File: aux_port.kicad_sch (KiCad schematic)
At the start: 29 parts, among them IC1 ECP5-BGA256, J5 MEZZANINE, U11 USB3343-CP, U12 FUSB302B, U14 DPO2036

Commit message: rename libraries from luna to cynthion
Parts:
- D15: footprint luna:DFN1006-2 -> cynthion:DFN1006-2
- IC1: footprint luna:lattice_cabga256 -> cynthion:lattice_cabga256
- J5: footprint luna:Amphenol_10132798-03 -> cynthion:Amphenol_10132798-03
- U14: footprint luna:Diodes_UQFN2020-12_Type-B -> cynthion:Diodes_UQFN2020-12_Type-B
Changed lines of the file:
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@@
     (property "Reference" "J5" (id 0) (at 92.71 57.2602 0))
     (property "Value" "MEZZANINE" (id 1) (at 92.71 59.7971 0))
-    (property "Footprint" "luna:Amphenol_10132798-03" (id 2) (at 93.98 80.01 0)
+    (property "Footprint" "cynthion:Amphenol_10132798-03" (id 2) (at 93.98 80.01 0)
       (effects (font (size 1.27 1.27)) hide)
     )
@@
     (property "Reference" "U14" (id 0) (at 233.045 61.121 0))
     (property "Value" "DPO2036" (id 1) (at 233.045 63.6579 0))
-    (property "Footprint" "luna:Diodes_UQFN2020-12_Type-B" (id 2) (at 233.045 73.66 0)
+    (property "Footprint" "cynthion:Diodes_UQFN2020-12_Type-B" (id 2) (at 233.045 73.66 0)
       (effects (font (size 1.27 1.27)) hide)
     )
@@
       (effects (font (size 1.27 1.27)) (justify right))
     )
-    (property "Footprint" "luna:lattice_cabga256" (id 2) (at -53.34 7.62 0)
+    (property "Footprint" "cynthion:lattice_cabga256" (id 2) (at -53.34 7.62 0)
       (effects (font (size 1.27 1.27)) (justify left) hide)
     )
@@
       (effects (font (size 1.27 1.27)) (justify left))
     )
-    (property "Footprint" "luna:DFN1006-2" (id 2) (at 240.665 35.56 0)
-      (effects (font (size 1.27 1.27)) hide)
-    )
+    (property "Footprint" "cynthion:DFN1006-2" (id 2) (at 240.665 35.56 0)
+      (effects (font (size 1.27 1.27)) hide)
+    )

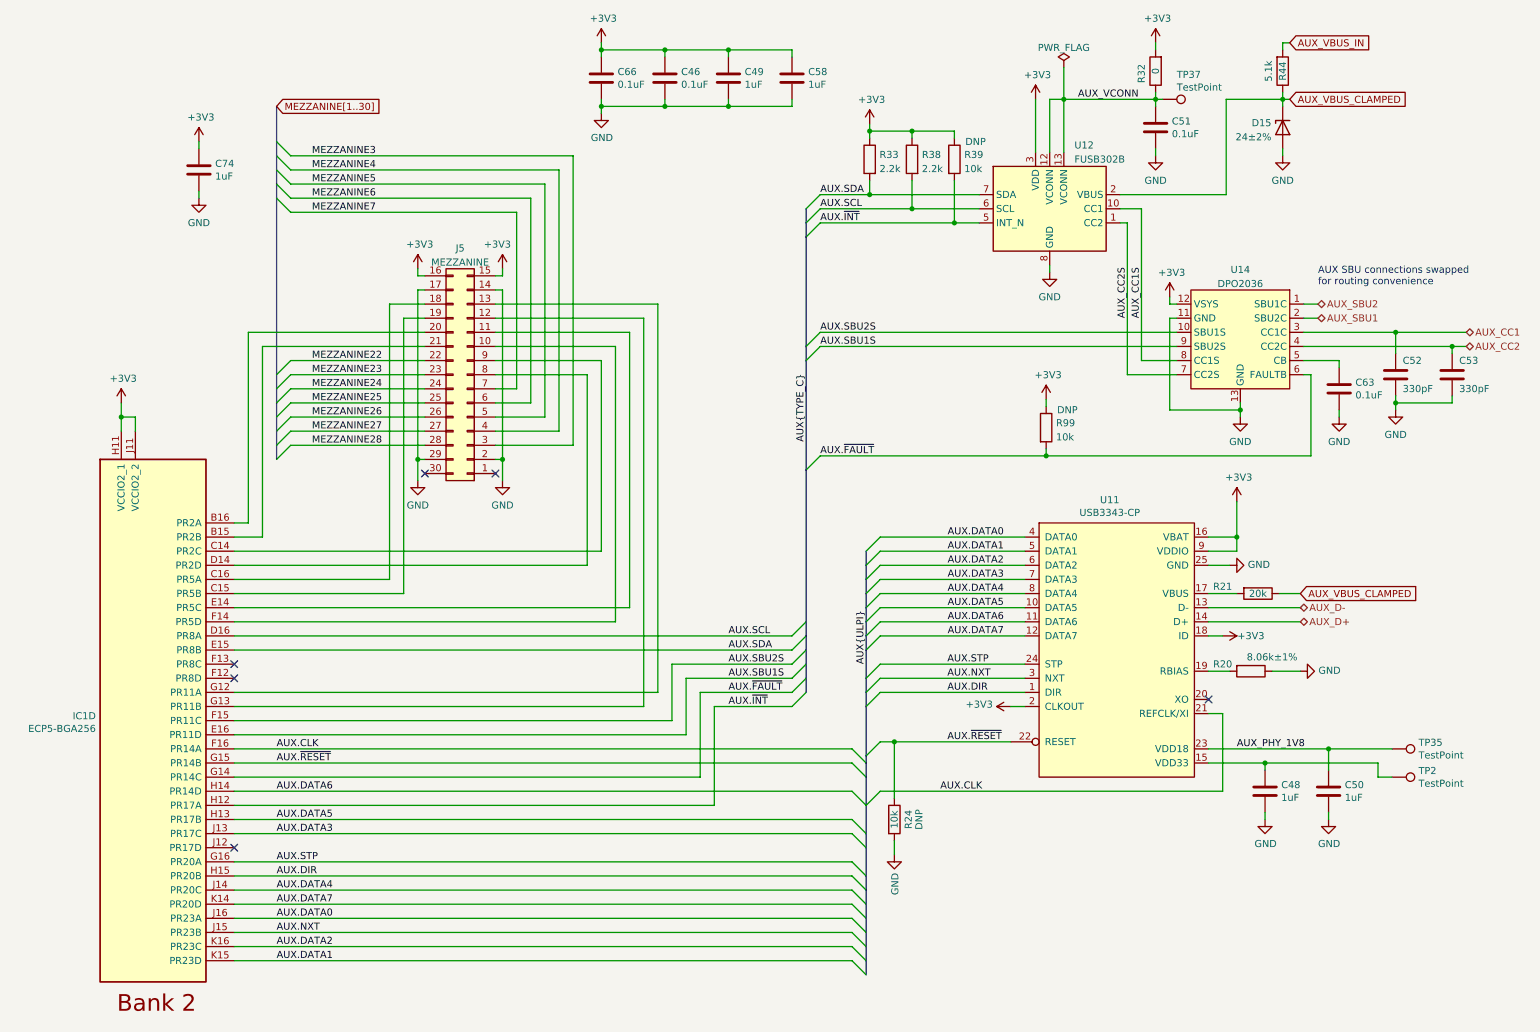
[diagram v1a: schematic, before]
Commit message: Move AUX ULPI signals to F.Cu
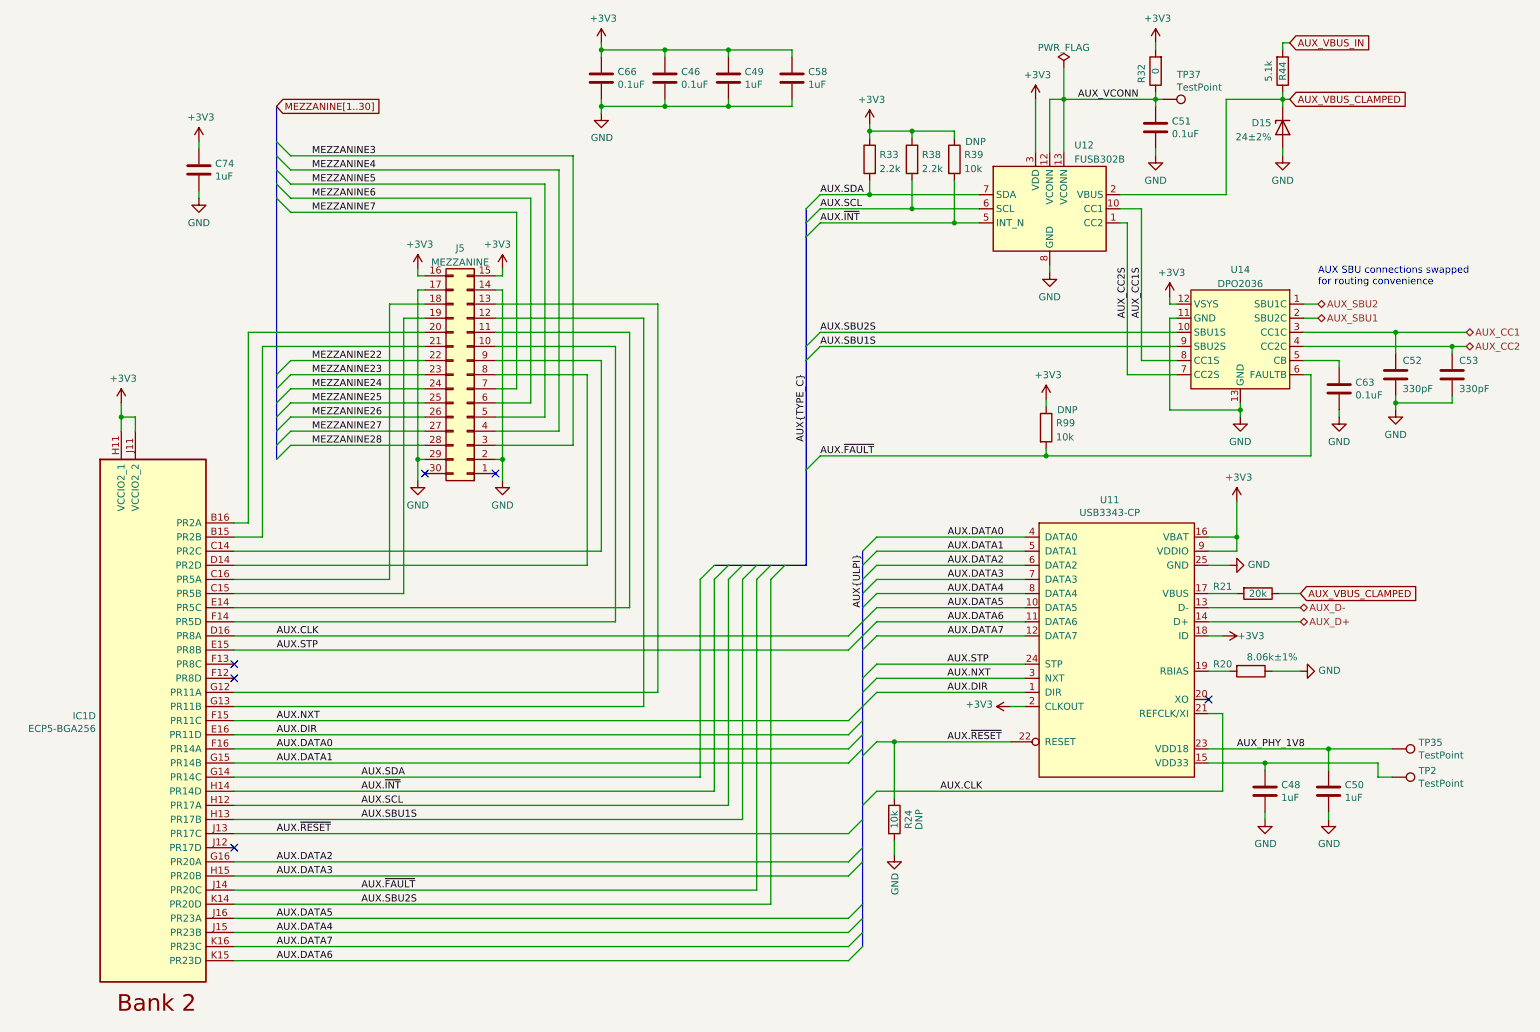
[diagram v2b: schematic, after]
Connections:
- net AUX.CLK: now also IC1.D16 (PR8A); no longer IC1.F16 (PR14A)
- net AUX.DATA0: now also IC1.F16 (PR14A); no longer IC1.J16 (PR23A)
- net AUX.DATA1: now also IC1.G15 (PR14B); no longer IC1.K15 (PR23D)
- net AUX.DATA2: now also IC1.G16 (PR20A); no longer IC1.K16 (PR23C)
- net AUX.DATA3: now also IC1.H15 (PR20B); no longer IC1.J13 (PR17C)
- net AUX.DATA4: now also IC1.J15 (PR23B); no longer IC1.J14 (PR20C)
- net AUX.DATA5: now also IC1.J16 (PR23A); no longer IC1.H13 (PR17B)
- net AUX.DATA6: now also IC1.K15 (PR23D); no longer IC1.H14 (PR14D)
- net AUX.DATA7: now also IC1.K16 (PR23C); no longer IC1.K14 (PR20D)
- net AUX.DIR: now also IC1.E16 (PR11D); no longer IC1.H15 (PR20B)
- net AUX.NXT: now also IC1.F15 (PR11C); no longer IC1.J15 (PR23B)
- net AUX.SBU1S: now also IC1.H13 (PR17B); no longer IC1.E16 (PR11D)
- net AUX.SBU2S: now also IC1.K14 (PR20D); no longer IC1.F15 (PR11C)
- net AUX.SCL: now also IC1.H12 (PR17A); no longer IC1.D16 (PR8A)
- net AUX.SDA: now also IC1.G14 (PR14C); no longer IC1.E15 (PR8B)
- net AUX.STP: now also IC1.E15 (PR8B); no longer IC1.G16 (PR20A)
- net AUX.~{FAULT}: now also IC1.J14 (PR20C); no longer IC1.G14 (PR14C)
- net AUX.~{INT}: now also IC1.H14 (PR14D); no longer IC1.H12 (PR17A)
- net AUX.~{RESET}: now also IC1.J13 (PR17C); no longer IC1.G15 (PR14B)

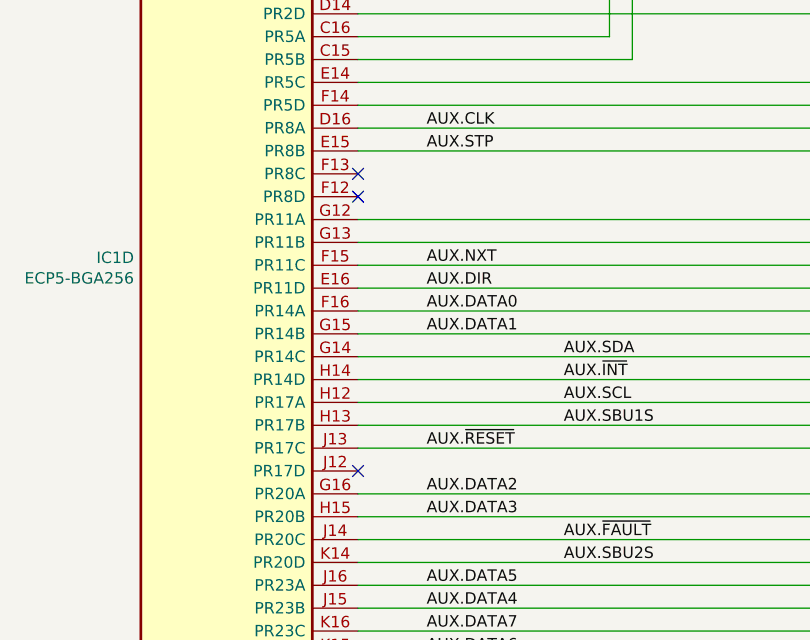
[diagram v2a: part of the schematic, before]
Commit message: Add pseudo-VCCIO and pseudo-GND pins, decoupling
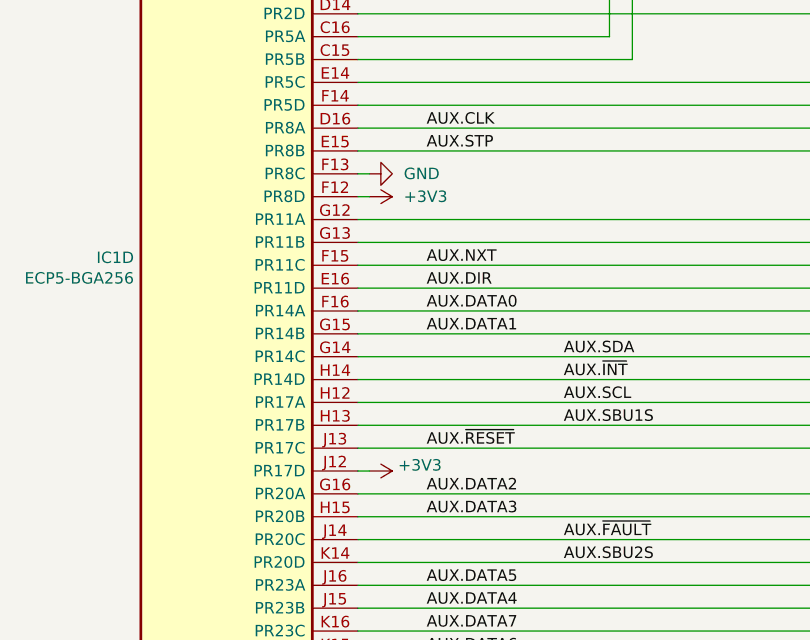
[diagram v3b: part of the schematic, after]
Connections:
- net +3V3: now also IC1.F12 (PR8D), IC1.J12 (PR17D)
- net GND: now also IC1.F13 (PR8C)
- no-connect marks 6 -> 3
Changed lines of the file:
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@@
   (junction (at 201.295 30.48) (diameter 0) (color 0 0 0 0)
   )
-  (no_connect (at 52.07 132.08))
-  (no_connect (at 52.07 165.1))
-  (no_connect (at 52.07 134.62))
   (no_connect (at 86.36 97.79))
   (no_connect (at 227.33 138.43))
@@
     (stroke (width 0) (type default) (color 0 0 0 0))
   )
+  (wire (pts (xy 52.07 132.08) (xy 53.34 132.08))
+    (stroke (width 0) (type default) (color 0 0 0 0))
+  )
   (wire (pts (xy 173.99 36.195) (xy 181.61 36.195))
     (stroke (width 0) (type default) (color 0 0 0 0))
@@
     (stroke (width 0) (type default) (color 0 0 0 0))
   )
+  (wire (pts (xy 52.07 134.62) (xy 53.34 134.62))
+    (stroke (width 0) (type default) (color 0 0 0 0))
+  )
   (wire (pts (xy 173.99 50.165) (xy 186.055 50.165))
     (stroke (width 0) (type default) (color 0 0 0 0))
@@
   )
   (bus (pts (xy 165.1 167.64) (xy 165.1 175.26))
+    (stroke (width 0) (type default) (color 0 0 0 0))
+  )
+  (wire (pts (xy 52.07 165.1) (xy 53.34 165.1))
     (stroke (width 0) (type default) (color 0 0 0 0))
   )
@@
     (pin "1")
     (pin "2")
+  )
+  (symbol (lib_id "power:+3V3") (at 53.34 134.62 270) (unit 1)
+    (in_bom yes) (on_board yes)
+    (property "Reference" "#PWR0179" (id 0) (at 49.53 134.62 0)
+      (effects (font (size 1.27 1.27)) hide)
+    )
+    (property "Value" "+3V3" (id 1) (at 57.15 134.62 90)
+      (effects (font (size 1.27 1.27)) (justify left))
+    )
+    (property "Footprint" "" (id 2) (at 53.34 134.62 0)
+      (effects (font (size 1.27 1.27)) hide)
+    )
+    (property "Datasheet" "" (id 3) (at 53.34 134.62 0)
+      (effects (font (size 1.27 1.27)) hide)
+    )
+    (pin "1")
   )
   (symbol (lib_id "Connector:TestPoint") (at 219.075 30.48 270) (unit 1)
@@
     (pin "2")
   )
+  (symbol (lib_id "power:+3V3") (at 53.34 165.1 270) (unit 1)
+    (in_bom yes) (on_board yes)
+    (property "Reference" "#PWR0177" (id 0) (at 49.53 165.1 0)
+      (effects (font (size 1.27 1.27)) hide)
+    )
+    (property "Value" "+3V3" (id 1) (at 56.515 164.465 90)
+      (effects (font (size 1.27 1.27)) (justify left))
+    )
+    (property "Footprint" "" (id 2) (at 53.34 165.1 0)
+      (effects (font (size 1.27 1.27)) hide)
+    )
+    (property "Datasheet" "" (id 3) (at 53.34 165.1 0)
+      (effects (font (size 1.27 1.27)) hide)
+    )
+    (pin "1")
+  )
   (symbol (lib_id "power:GND") (at 250.825 87.63 0) (mirror y) (unit 1)
     (in_bom yes) (on_board yes) (fields_autoplaced)
@@
       (effects (font (size 1.27 1.27)) hide)
     )
+    (pin "1")
+  )
+  (symbol (lib_id "power:GND") (at 53.34 132.08 90) (unit 1)
+    (in_bom yes) (on_board yes)
+    (property "Reference" "#PWR0178" (id 0) (at 59.69 132.08 0)
+      (effects (font (size 1.27 1.27)) hide)
+    )
+    (property "Value" "GND" (id 1) (at 57.15 132.08 90)
+      (effects (font (size 1.27 1.27)) (justify right))
+    )
+    (property "Footprint" "" (id 2) (at 53.34 132.08 0)
+      (effects (font (size 1.27 1.27)) hide)
+    )
+    (property "Datasheet" "" (id 3) (at 53.34 132.08 0)
+      (effects (font (size 1.27 1.27)) hide)
+    )
